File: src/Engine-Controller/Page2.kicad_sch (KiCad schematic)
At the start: 24 parts, among them P2 Solid Prop Cont, P4 Micro_SD_Card, P5 USB, Q1 QS5U17TR, U4 SST25VF040B-50-4I-S2AE-T, U5 CP2102-GMR(QFN28)

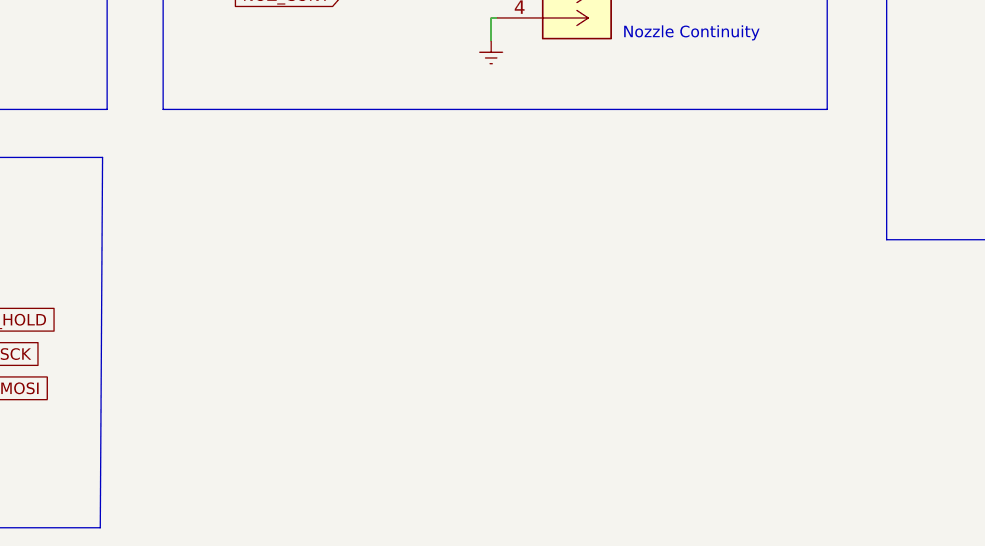
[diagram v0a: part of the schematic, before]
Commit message: Added connectors for valve controller and main power line
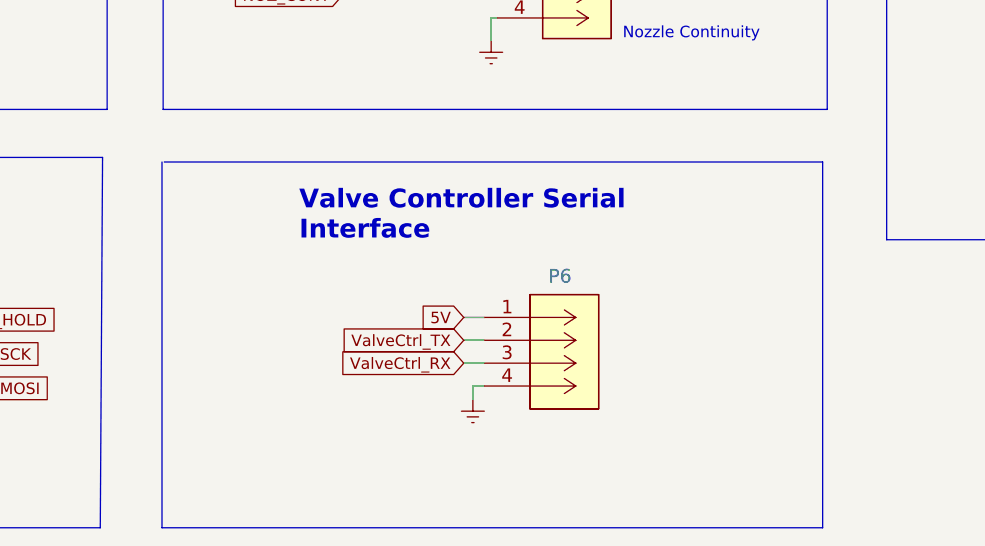
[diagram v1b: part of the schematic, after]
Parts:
- added P6: 140-504-415-000, CONN_4840.2201_SCH, symbol Engine-Controller:140-504-415-000
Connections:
- net Earth: now also P6.4
- new net 5V: P6.1 (+12V)
- new net ValveCtrl_RX: P6.3
- new net ValveCtrl_TX: P6.2 (GND)
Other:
- note added: "Valve Controller Serial Interface"
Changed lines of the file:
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@@
+    (stroke (width 0) (type default) (color 0 0 0 0))
+  )
+  (wire (pts (xy 129.54 174.498) (xy 131.826 174.498))
     (stroke (width 0) (type default) (color 0 0 0 0))
   )
@@
     (stroke (width 0) (type default) (color 0 0 0 0))
   )
+  (polyline (pts (xy 96.266 152.146) (xy 169.418 152.146))
+    (stroke (width 0) (type default) (color 0 0 0 0))
+  )
   (polyline (pts (xy 20.066 101.854) (xy 89.916 101.854))
     (stroke (width 0) (type default) (color 0 0 0 0))
@@
     (stroke (width 0) (type default) (color 0 0 0 0))
   )
+  (polyline (pts (xy 169.418 152.146) (xy 169.418 192.786))
+    (stroke (width 0) (type default) (color 0 0 0 0))
+  )
   (wire (pts (xy 57.531 126.619) (xy 53.086 126.619))
     (stroke (width 0) (type default) (color 0 0 0 0))
@@
     (stroke (width 0) (type default) (color 0 0 0 0))
   )
+  (polyline (pts (xy 96.012 152.146) (xy 96.012 192.786))
+    (stroke (width 0) (type default) (color 0 0 0 0))
+  )
   (wire (pts (xy 235.966 76.2) (xy 235.966 81.28))
     (stroke (width 0) (type default) (color 0 0 0 0))
@@
     (stroke (width 0) (type default) (color 0 0 0 0))
   )
+  (wire (pts (xy 129.54 169.418) (xy 131.826 169.418))
+    (stroke (width 0) (type default) (color 0 0 0 0))
+  )
+  (wire (pts (xy 130.556 177.038) (xy 130.556 178.562))
+    (stroke (width 0) (type default) (color 0 0 0 0))
+  )
   (polyline (pts (xy 176.53 101.854) (xy 176.53 160.782))
     (stroke (width 0) (type default) (color 0 0 0 0))
@@
     (stroke (width 0) (type default) (color 0 0 0 0))
   )
+  (wire (pts (xy 131.826 177.038) (xy 130.556 177.038))
+    (stroke (width 0) (type default) (color 0 0 0 0))
+  )
   (polyline (pts (xy 276.86 18.288) (xy 276.86 96.774))
     (stroke (width 0) (type default) (color 0 0 0 0))
@@
     (stroke (width 0) (type default) (color 0 0 0 0))
   )
+  (wire (pts (xy 129.54 171.958) (xy 131.826 171.958))
+    (stroke (width 0) (type default) (color 0 0 0 0))
+  )
   (polyline (pts (xy 20.066 146.304) (xy 20.066 101.854))
     (stroke (width 0) (type default) (color 0 0 0 0))
@@
   )
   (polyline (pts (xy 276.606 160.782) (xy 176.53 160.782))
+    (stroke (width 0) (type default) (color 0 0 0 0))
+  )
+  (polyline (pts (xy 169.418 192.786) (xy 96.012 192.786))
     (stroke (width 0) (type default) (color 0 0 0 0))
   )
@@
     (effects (font (size 1.27 1.27)) (justify left bottom))
   )
+  (text "Valve Controller Serial\nInterface" (at 111.252 161.036 0)
+    (effects (font (size 2.08 2.08) (thickness 0.416) bold) (justify left bottom))
+  )
   (label "D+" (at 198.501 57.15 0)
     (effects (font (size 1.27 1.27)) (justify left bottom))
@@
     (property "Intersheet References" "${INTERSHEET_REFS}" (id 0) (at -119.126 -44.196 0)
       (effects (font (size 1.27 1.27)) hide)
+    )
+  )
+  (global_label "5V" (shape input) (at 129.54 169.418 180) (fields_autoplaced)
+    (effects (font (size 1.27 1.27)) (justify right))
+    (property "Intersheet References" "${INTERSHEET_REFS}" (id 0) (at 124.9177 169.3386 0)
+      (effects (font (size 1.27 1.27)) (justify right) hide)
+    )
+  )
+  (global_label "ValveCtrl_TX" (shape input) (at 129.54 171.958 180) (fields_autoplaced)
+    (effects (font (size 1.27 1.27)) (justify right))
+    (property "Intersheet References" "${INTERSHEET_REFS}" (id 0) (at 115.6648 171.8786 0)
+      (effects (font (size 1.27 1.27)) (justify right) hide)
     )
   )
@@
     )
   )
+  (global_label "ValveCtrl_RX" (shape input) (at 129.54 174.498 180) (fields_autoplaced)
+    (effects (font (size 1.27 1.27)) (justify right))
+    (property "Intersheet References" "${INTERSHEET_REFS}" (id 0) (at 115.3625 174.4186 0)
+      (effects (font (size 1.27 1.27)) (justify right) hide)
+    )
+  )
   (global_label "NOZ_CONT" (shape input) (at 116.078 133.604 180) (fields_autoplaced)
     (effects (font (size 1.27 1.27)) (justify right))
@@
     (pin "1")
     (pin "2")
+  )
+  (symbol (lib_name "Earth_1") (lib_id "Engine-Controller:Earth") (at 130.556 178.562 0) (unit 1)
+    (in_bom yes) (on_board yes) (fields_autoplaced)
+    (property "Reference" "#PWR028" (id 0) (at 130.556 184.912 0)
+      (effects (font (size 1.27 1.27)) hide)
+    )
+    (property "Value" "Earth" (id 1) (at 130.556 182.372 0)
+      (effects (font (size 1.27 1.27)) hide)
+    )
+    (property "Footprint" "" (id 2) (at 130.556 178.562 0)
+      (effects (font (size 1.27 1.27)) hide)
+    )
+    (property "Datasheet" "" (id 3) (at 130.556 178.562 0)
+      (effects (font (size 1.27 1.27)) hide)
+    )
+    (pin "1")
   )
   (symbol (lib_id "Engine-Controller:Earth") (at 73.406 133.604 0) (unit 1)
@@
   (symbol (lib_id "Engine-Controller:Earth") (at 218.186 64.262 0) (unit 1)
     (in_bom yes) (on_board yes)
-    (property "Reference" "#PWR?" (id 0) (at 218.186 70.612 0)
+    (property "Reference" "#PWR029" (id 0) (at 218.186 70.612 0)
       (effects (font (size 1.27 1.27)) hide)
     )
@@
     (pin "1")
   )
+  (symbol (lib_id "Engine-Controller:140-504-415-000") (at 131.826 169.418 0) (unit 1)
+    (in_bom yes) (on_board yes)
+    (property "Reference" "P6" (id 0) (at 138.938 164.846 0)
+      (effects (font (size 1.524 1.524)) (justify left))
+    )
+    (property "Value" "140-504-415-000" (id 1) (at 140.716 180.848 0)
+      (effects (font (size 1.524 1.524)) hide)
+    )
+    (property "Footprint" "CONN_4840.2201_SCH" (id 2) (at 141.986 184.658 0)
+      (effects (font (size 1.524 1.524)) hide)
+    )
+    (property "Datasheet" "" (id 3) (at 131.826 169.418 0)
+      (effects (font (size 1.524 1.524)))
+    )
+    (pin "1")
+    (pin "2")
+    (pin "3")
+    (pin "4")
+  )
   (symbol (lib_id "Engine-Controller:Earth") (at 166.624 72.136 0) (unit 1)

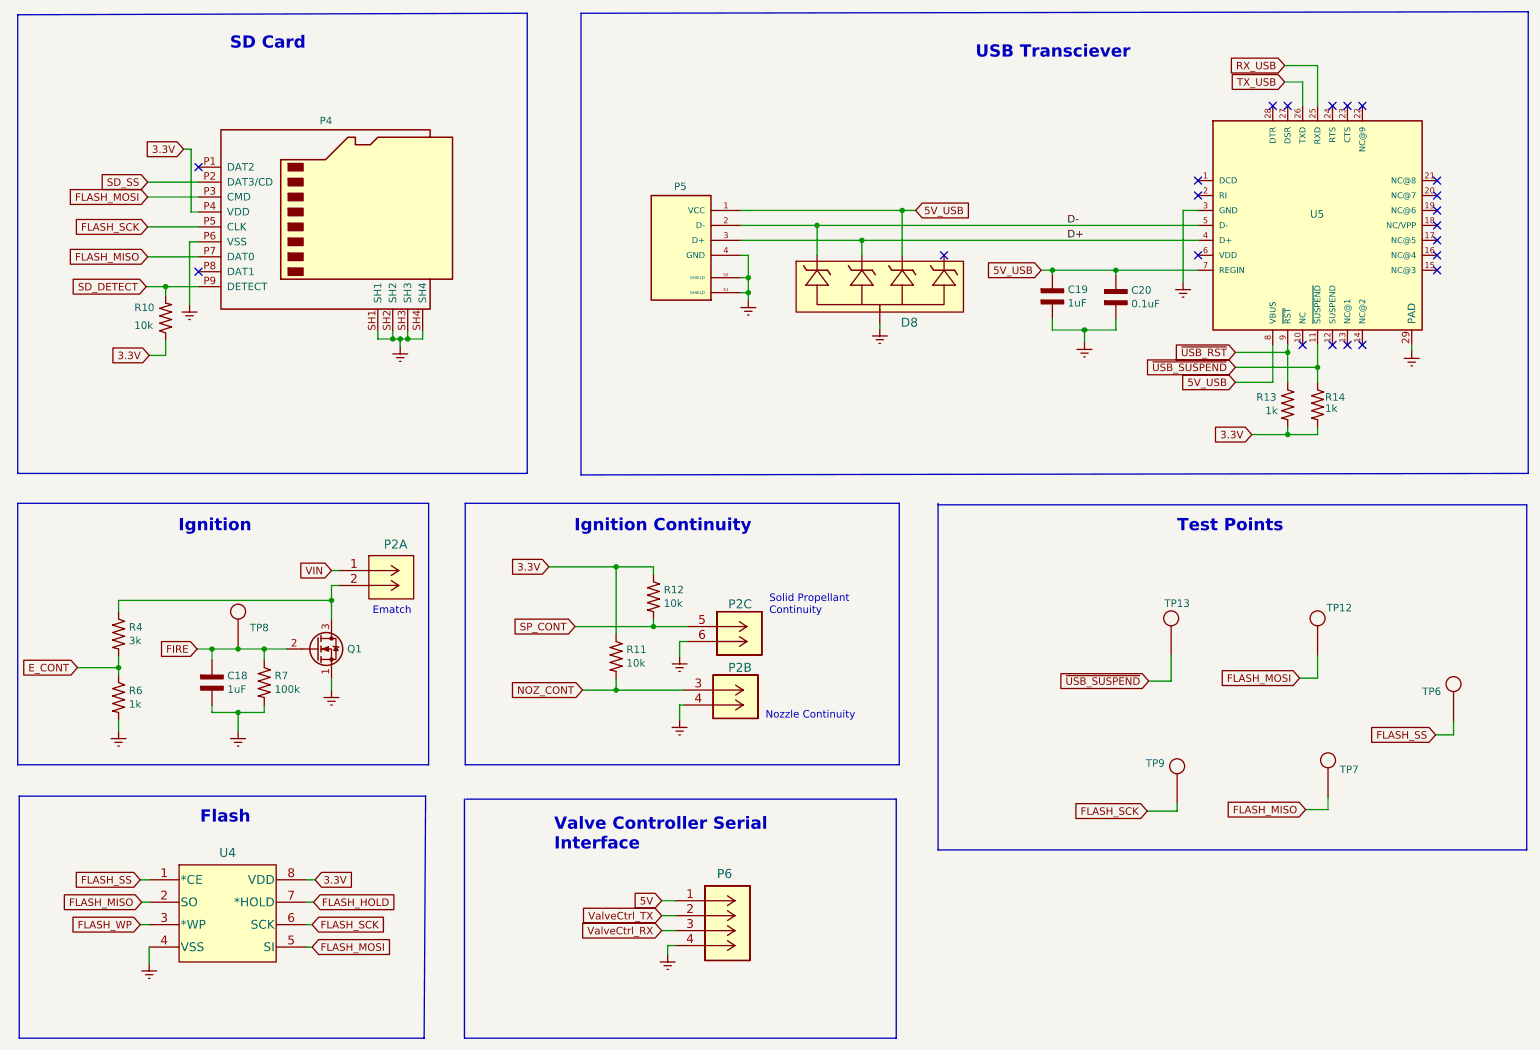
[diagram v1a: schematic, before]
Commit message: updated test points and USB resistors
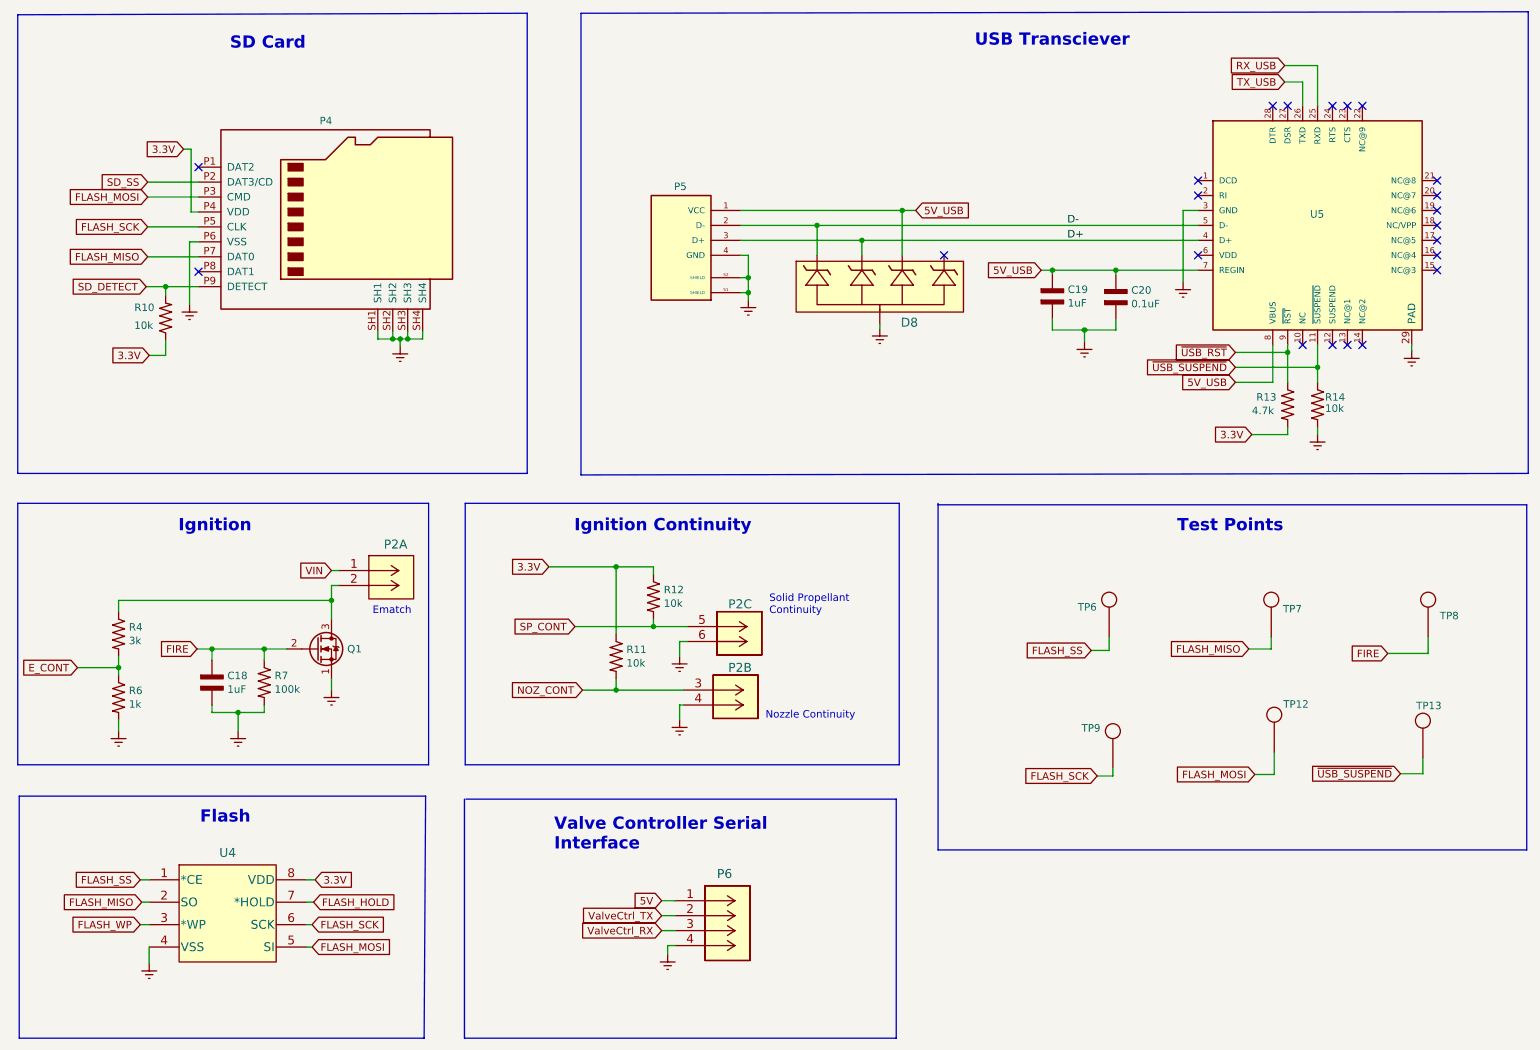
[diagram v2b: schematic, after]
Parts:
- R13: value 1k -> 4.7k
- R14: value 1k -> 10k
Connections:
- net 3.3V: no longer R14.2
- net Earth: now also R14.2
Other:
- moved on the sheet: TP12, TP13, TP6, TP7, TP8, TP9

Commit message: moved schematic components to 25 mil grid
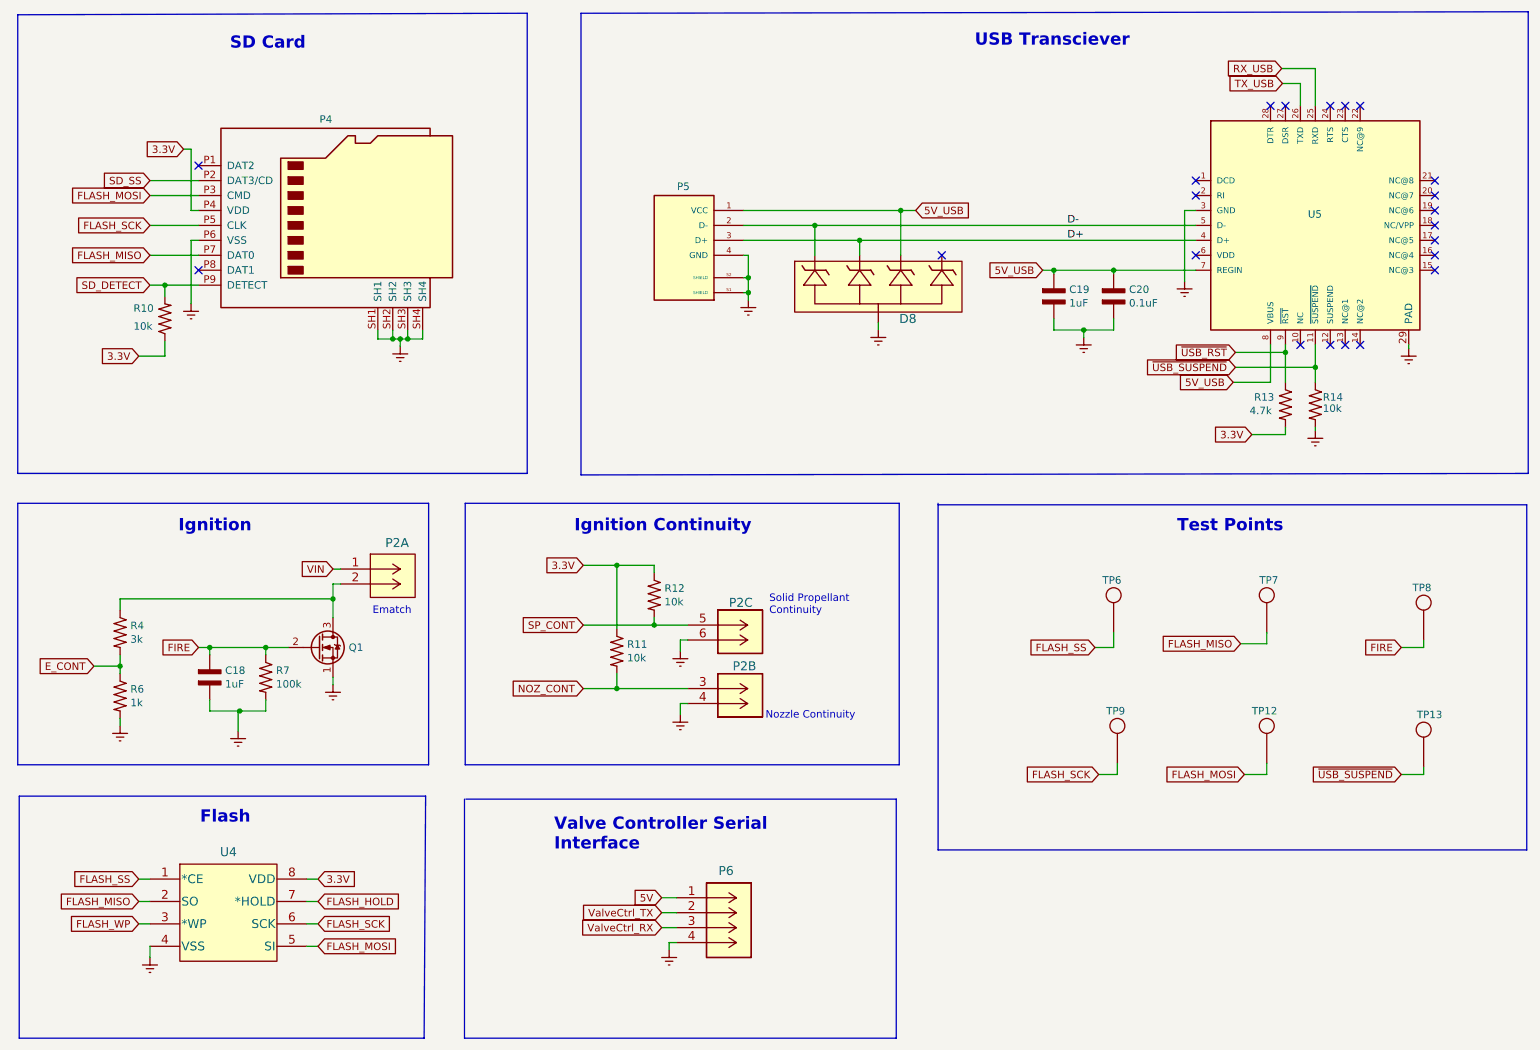
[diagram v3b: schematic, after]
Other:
- moved on the sheet: C18, P2B, P5, P6, R11, R7, TP12, TP13, TP6, TP7, TP8, TP9
